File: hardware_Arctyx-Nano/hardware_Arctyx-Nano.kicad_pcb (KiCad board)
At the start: 4 copper layers, 21 x 51 mm, 73 parts, among them J1 USB_C_Receptacle_USB2.0_16P, J2 Conn_01x20_Pin, J3 Conn_01x20_Pin, SW1 SW_Push, U1 ICE40UP5K-SG48ITR, U2 RP2350A-QFN60, U3 W25Q128JVP, U4 RT8075ZQW, U5 TJ-S1608SW6TDSLCCYRGB-A5, Y1 Crystal_GND24

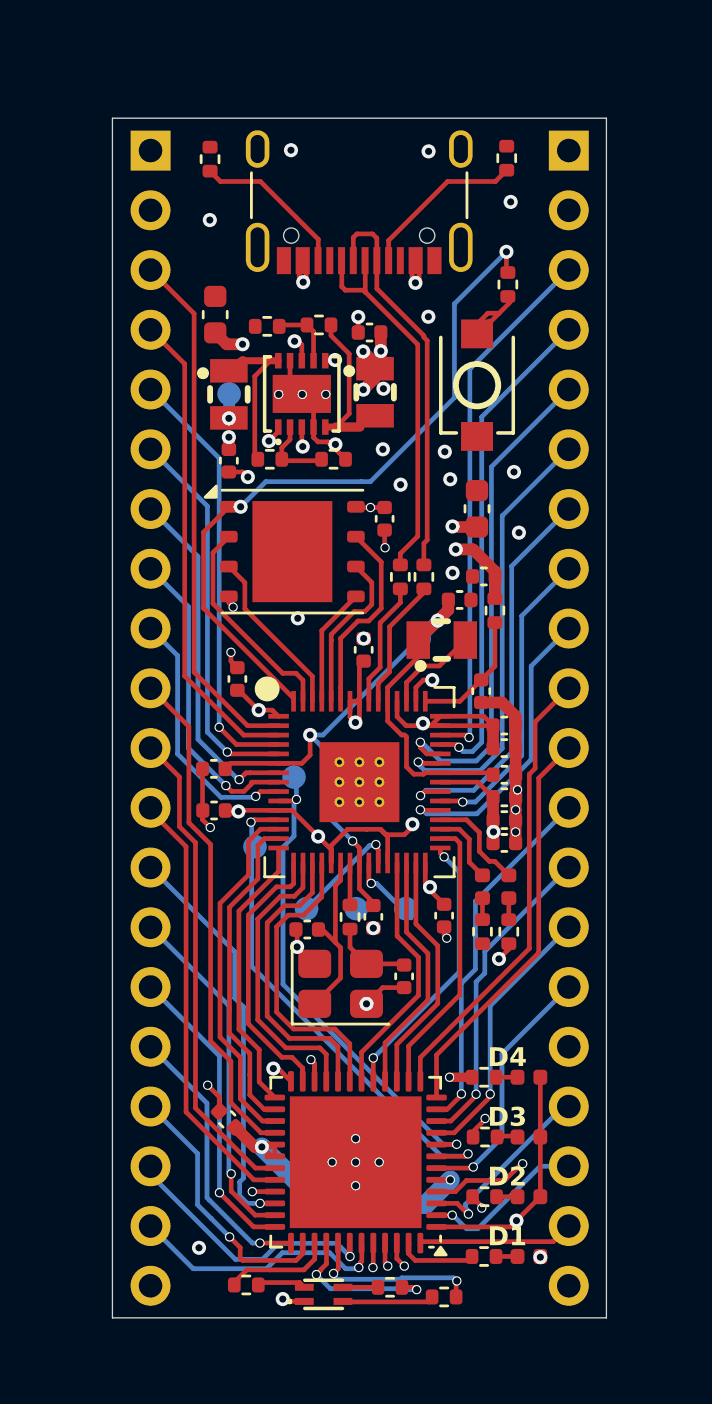
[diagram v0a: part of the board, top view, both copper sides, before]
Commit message: PCB fixing errors
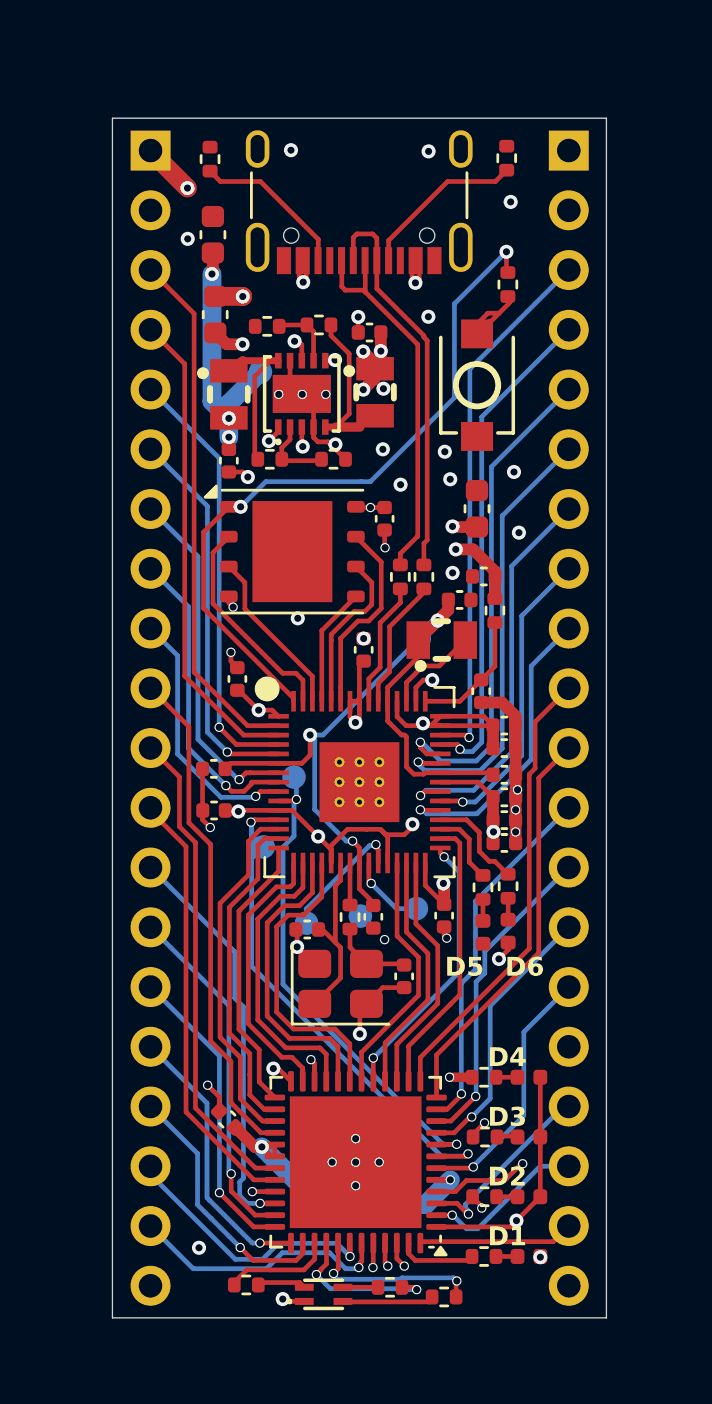
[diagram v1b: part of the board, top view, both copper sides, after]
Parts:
- added C24: 10u, Capacitor_SMD:C_0603_1608Metric, F.Cu at (154.3, 55.0)
- moved D5 2.23 mm to (165.8, 84.6)
- moved D6 2.18 mm to (166.8, 84.6)
- moved R20 1.93 mm to (166.8, 82.7)
- moved R21 1.88 mm to (165.8, 82.7)
- moved TP7 1.62 mm to (156.3, 60.8)
- moved TP3 0.62 mm to (158.3, 84.2)
- moved TP1 0.45 mm to (162.9, 83.6)
- moved TP2 0.36 mm to (160.5, 83.9)
- moved TP5 0.35 mm to (156.4, 81.0)
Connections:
- D5 pad 1: Net-(D5-K) -> GND
- D6 pad 1: Net-(D6-K) -> GND
- R20 pad 1: GND -> Net-(D6-A)
- R20 pad 2: Net-(D5-K) -> Net-(U2-GPIO22)
- R21 pad 1: GND -> Net-(D5-A)
- R21 pad 2: Net-(D6-K) -> Net-(U2-GPIO21)
- U2 pad 33: Net-(D6-A) -> Net-(U2-GPIO21)
- U2 pad 34: Net-(D5-A) -> Net-(U2-GPIO22)
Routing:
- net VBUS: track 11.8 -> 22.7 mm, vias 6 -> 7
- net 1v2: track 59.7 -> 68.5 mm, vias 5 -> 6
- net Net-(U2-GPIO22): track 0.00 -> 4.36 mm
- net Net-(D5-A): track 4.36 -> 0.92 mm
- net Net-(U2-GPIO21): track 0.00 -> 3.18 mm
- net GND: track 26.1 -> 28.7 mm, vias 40 -> 41
- net Net-(D6-A): track 3.18 -> 0.92 mm
- net CDONE: track 21.3 -> 23.6 mm
- net Net-(D5-K): track 0.99 -> 0.00 mm
- net Net-(D6-K): track 0.92 -> 0.00 mm
- net 3v3: track 61.1 -> 61.7 mm
- net Net-(U2-SWDIO): track 4.90 -> 5.52 mm
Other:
- board text added: "3v3"
- board text added: "D5"
- board text added: "D6"
- board text added: "GND"
- board text added: "GP0"
- board text added: "GP1"
- board text added: "GP2"
- board text added: "GP23"
- board text added: "GP24"
- board text added: "GP25"
- board text added: "GP26"
- board text added: "GP27"
- board text added: "GP28"
- board text added: "GP29"
- board text added: "GP3"
- board text added: "GP4"
- board text added: "GP5"
- board text added: "GP6"
- board text added: "IO1"
- board text added: "IO10"
- board text added: "IO11"
- board text added: "IO12"
- board text added: "IO13"
- board text added: "IO14"
- board text added: "IO15"
- board text added: "IO16"
- board text added: "IO17"
- board text added: "IO18"
- board text added: "IO19"
- board text added: "IO2"
- board text added: "IO20"
- board text added: "IO3"
- board text added: "IO4"
- board text added: "IO5"
- board text added: "IO6"
- board text added: "IO7"
- board text added: "IO8"
- board text added: "IO9"
- board text added: "VBUS"

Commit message: production files generation and branding
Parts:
- added G***: LOGO, LOGO, F.Cu at (149.3, 70.2)
- R11: value 51k -> 100k
- R12: value R -> 22k
- moved R15 36.1 mm to (135.2, 78.4), turned to -90 degrees
- moved R13 35.7 mm to (135.7, 70.0), turned to 90 degrees
- moved U5 35.7 mm to (135.3, 73.3), turned to -90 degrees
- moved J3 35.5 mm to (183.9, 83.7), turned to 90 degrees
- moved J2 35.4 mm to (183.9, 65.9), turned to 90 degrees
- moved R14 35.2 mm to (135.6, 76.1), turned to -90 degrees
- moved D1 34.9 mm to (136.9, 82.0), turned to -90 degrees
- moved R16 34.2 mm to (136.9, 80.1), turned to -90 degrees
- moved R1 33.9 mm to (183.6, 81.1), turned to 0 degrees
- moved R2 33.8 mm to (183.6, 68.5), turned to 0 degrees
- moved J1 31.7 mm to (182.9, 74.8), turned to 90 degrees
- moved D2 31.5 mm to (139.5, 82.0), turned to -90 degrees
- moved R17 30.7 mm to (139.5, 80.1), turned to -90 degrees
- moved C24 29.4 mm to (180.4, 68.6), turned to 0 degrees
- moved D3 28.1 mm to (142.0, 82.0), turned to -90 degrees
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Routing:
- net GND: track 28.7 -> 31.8 mm
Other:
- board size 21 x 51 mm -> 51 x 21 mm
- board text added: "Keyaan Was Here"

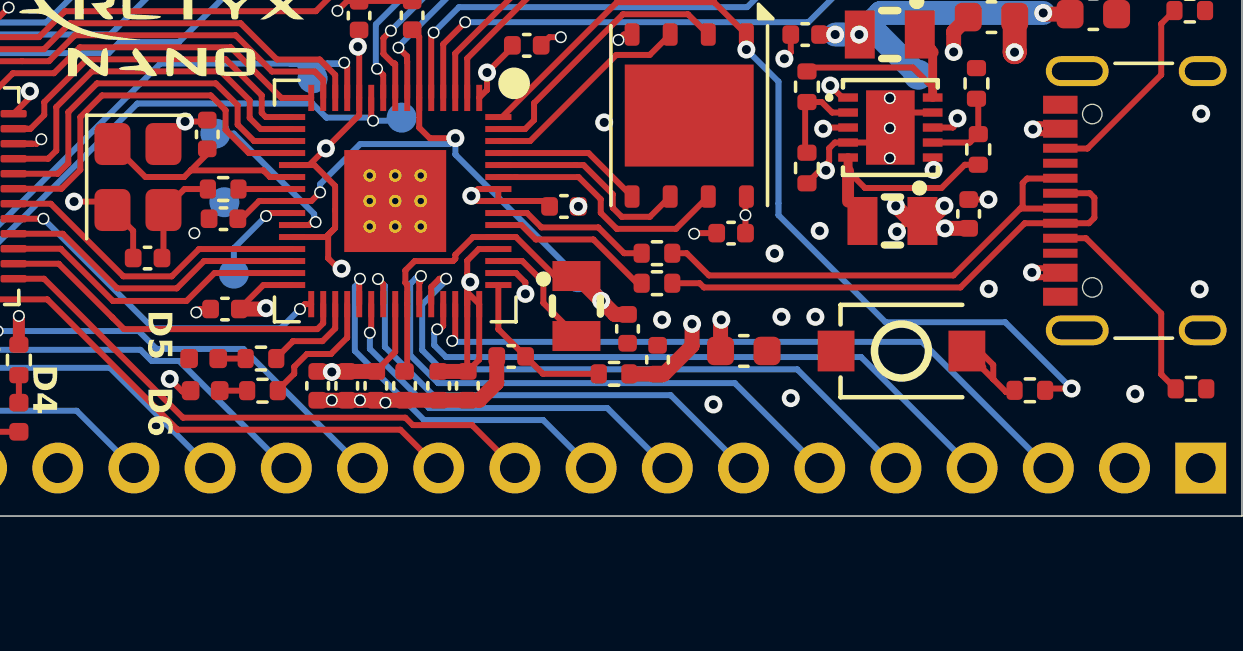
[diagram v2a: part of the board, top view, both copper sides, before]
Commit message: fixing rp2350 footprint
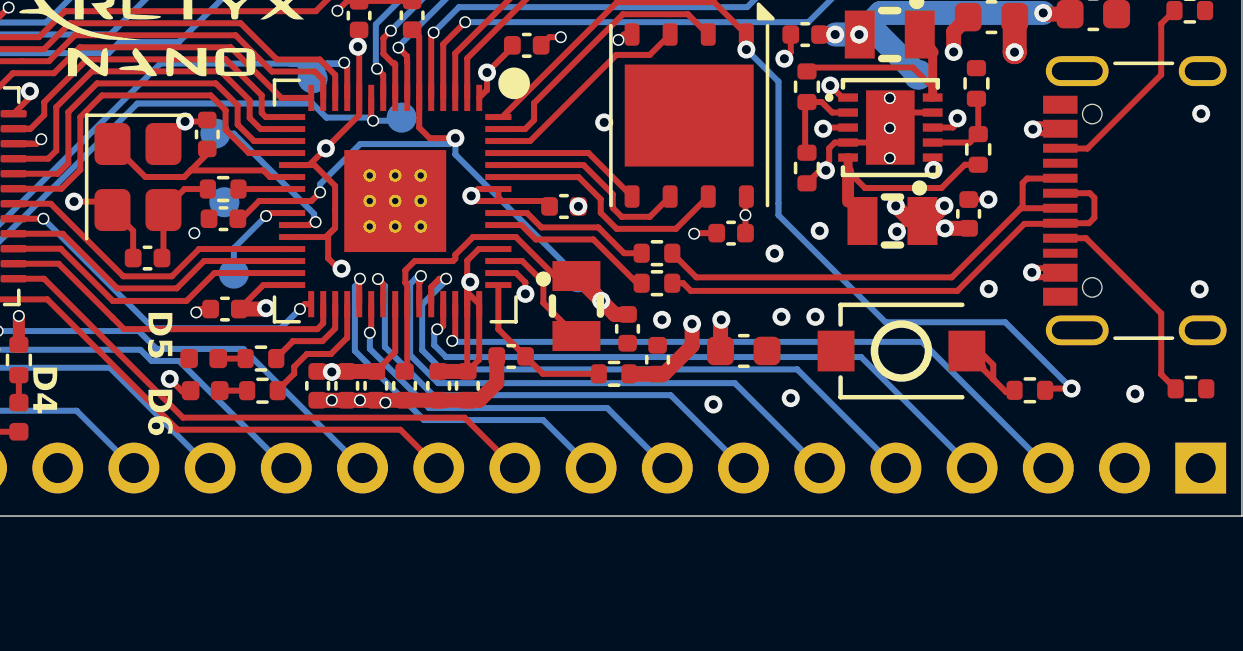
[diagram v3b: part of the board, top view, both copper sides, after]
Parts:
- removed ? (x4): , 
